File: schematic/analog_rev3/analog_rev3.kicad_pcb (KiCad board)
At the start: 2 copper layers, 50.8 x 107.9 mm, 202 parts, among them J1 Jack, J10 Jack, J11 Jack, J12 Jack, J13 Jack, J14 Jack, J15 Jack, J16 Jack, J17 Jack, J18 Jack, J19 Jack, J2 Jack, J20 Jack, J21 OLED Display, J22 Conn_02x07, J23 Conn_02x07, J24 Trigger Inputs, J25 Trigger Inputs, J26 Conn_01x16, J27 Conn_01x16, J3 Jack, J4 Jack, J5 Jack, J6 Jack, J7 Jack, J8 Jack, J9 Jack, SW1 SW_Push, SW2 SW_Push, SW3 SW_Push, SW4 SW_Push, SW5 SW_Push, SW6 Encoder, SW7 Encoder, U1 LM339, U10 MCP6022, U11 LM833, U2 MCP6002, U3 MCP6002, U4 MCP6002, U5 MCP6002, U6 OPA2172, U7 OPA2172, U8 OPA2172, U9 OPA2172

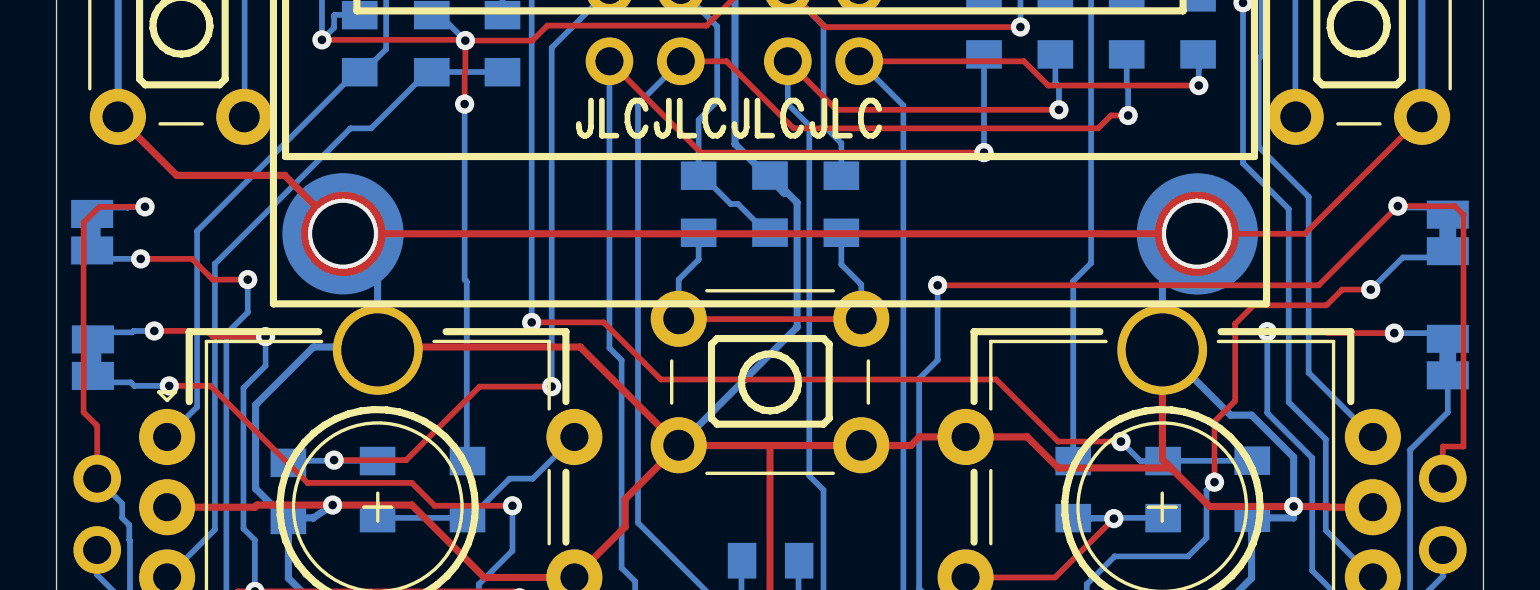
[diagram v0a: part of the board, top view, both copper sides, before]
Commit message: added D6 per Paul's recommendation, to help protect U17
reduced pads on ADC footprint to help prevent solder bridging

updated a few footprint silkscreens to look more like original rev3 board

generated updated gerber zip files

TODO: update IC pads to match more closely to original rev3 board if it makes soldering easier
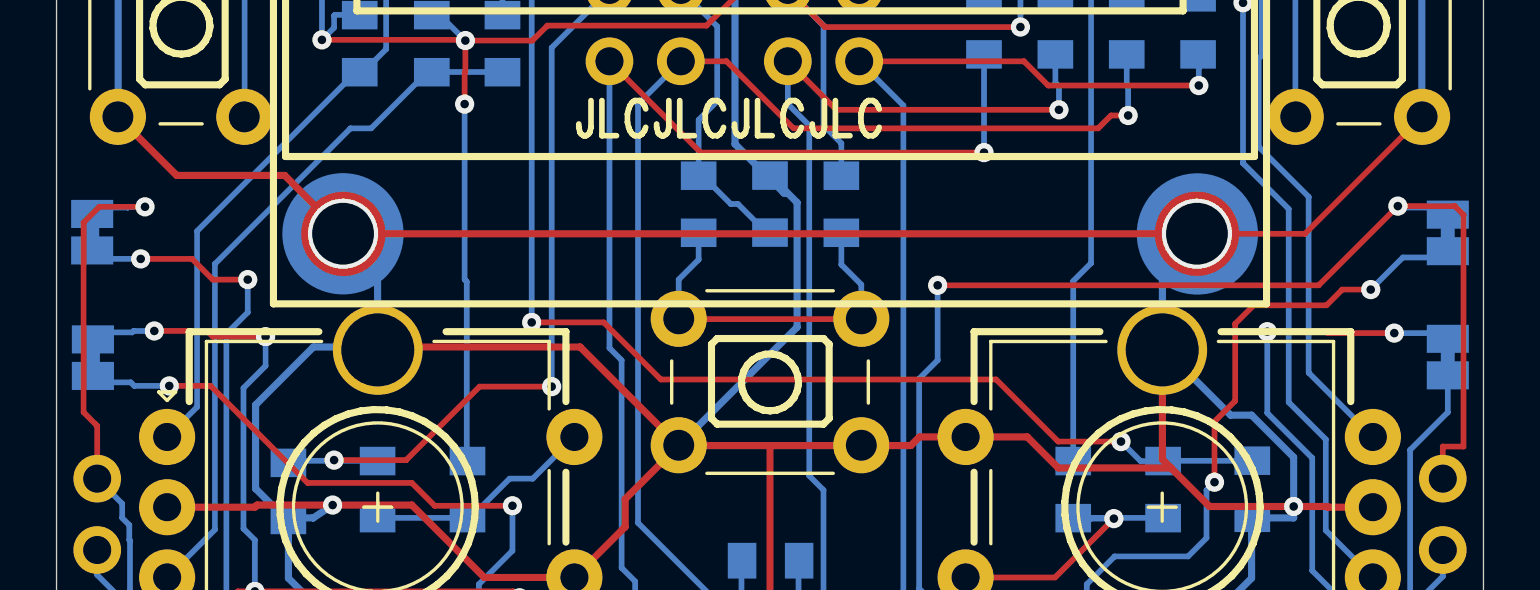
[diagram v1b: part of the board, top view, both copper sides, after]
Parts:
- JP1, JP2, JP3, JP4: footprint Jumper:SolderJumper-2_P1.3mm_Bridged_Pad1.0x1.5mm -> Custom_Footprints:SolderJumper-2_P1.3mm_Bridged_Pad1.0x1.5mm_reduced
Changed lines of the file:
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@@
 			(disableapertmacros no)
 			(usegerberextensions yes)
-			(usegerberattributes yes)
+			(usegerberattributes no)
 			(usegerberadvancedattributes yes)
 			(creategerberjobfile no)
@@
 			(drillshape 0)
 			(scaleselection 1)
-			(outputdirectory "../../pcb/gerber/")
+			(outputdirectory "../../pcb/gerber/export/")
 		)
 	)
@@
 		)
 	)
-	(footprint "Jumper:SolderJumper-2_P1.3mm_Bridged_Pad1.0x1.5mm"
+	(footprint "Custom_Footprints:SolderJumper-2_P1.3mm_Bridged_Pad1.0x1.5mm_reduced"
 		(layer "B.Cu")
 		(at 74.93 56.911 -90)
@@
 		(fp_poly
 			(pts
-				(xy -0.25 0.3) (xy 0.25 0.3) (xy 0.25 -0.3) (xy -0.25 -0.3)
+				(xy -0.25 0.2492) (xy 0.25 0.2492) (xy 0.25 -0.2492) (xy -0.25 -0.2492)
 			)
 			(stroke
@@
 		)
 	)
-	(footprint "Jumper:SolderJumper-2_P1.3mm_Bridged_Pad1.0x1.5mm"
+	(footprint "Custom_Footprints:SolderJumper-2_P1.3mm_Bridged_Pad1.0x1.5mm_reduced"
 		(layer "B.Cu")
 		(at 26.6954 61.3514 -90)
@@
 		(fp_poly
 			(pts
-				(xy -0.25 0.3) (xy 0.25 0.3) (xy 0.25 -0.3) (xy -0.25 -0.3)
+				(xy -0.25 0.2492) (xy 0.25 0.2492) (xy 0.25 -0.2492) (xy -0.25 -0.2492)
 			)
 			(stroke
@@
 		)
 	)
-	(footprint "Jumper:SolderJumper-2_P1.3mm_Bridged_Pad1.0x1.5mm"
+	(footprint "Custom_Footprints:SolderJumper-2_P1.3mm_Bridged_Pad1.0x1.5mm_reduced"
 		(layer "B.Cu")
 		(at 74.93 61.3306 -90)
@@
 		(fp_poly
 			(pts
-				(xy -0.25 0.3) (xy 0.25 0.3) (xy 0.25 -0.3) (xy -0.25 -0.3)
+				(xy -0.25 0.2492) (xy 0.25 0.2492) (xy 0.25 -0.2492) (xy -0.25 -0.2492)
 			)
 			(stroke
@@
 		)
 	)
-	(footprint "Jumper:SolderJumper-2_P1.3mm_Bridged_Pad1.0x1.5mm"
+	(footprint "Custom_Footprints:SolderJumper-2_P1.3mm_Bridged_Pad1.0x1.5mm_reduced"
 		(layer "B.Cu")
 		(at 26.67 56.8856 -90)
@@
 		(fp_poly
 			(pts
-				(xy -0.25 0.3) (xy 0.25 0.3) (xy 0.25 -0.3) (xy -0.25 -0.3)
+				(xy -0.25 0.2492) (xy 0.25 0.2492) (xy 0.25 -0.2492) (xy -0.25 -0.2492)
 			)
 			(stroke
